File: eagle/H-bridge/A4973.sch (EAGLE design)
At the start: 13 parts, among them IC1 A4973DIL, X1 Load, X2 V_Load, X3 MODE, X4 332-02, X5 332-02

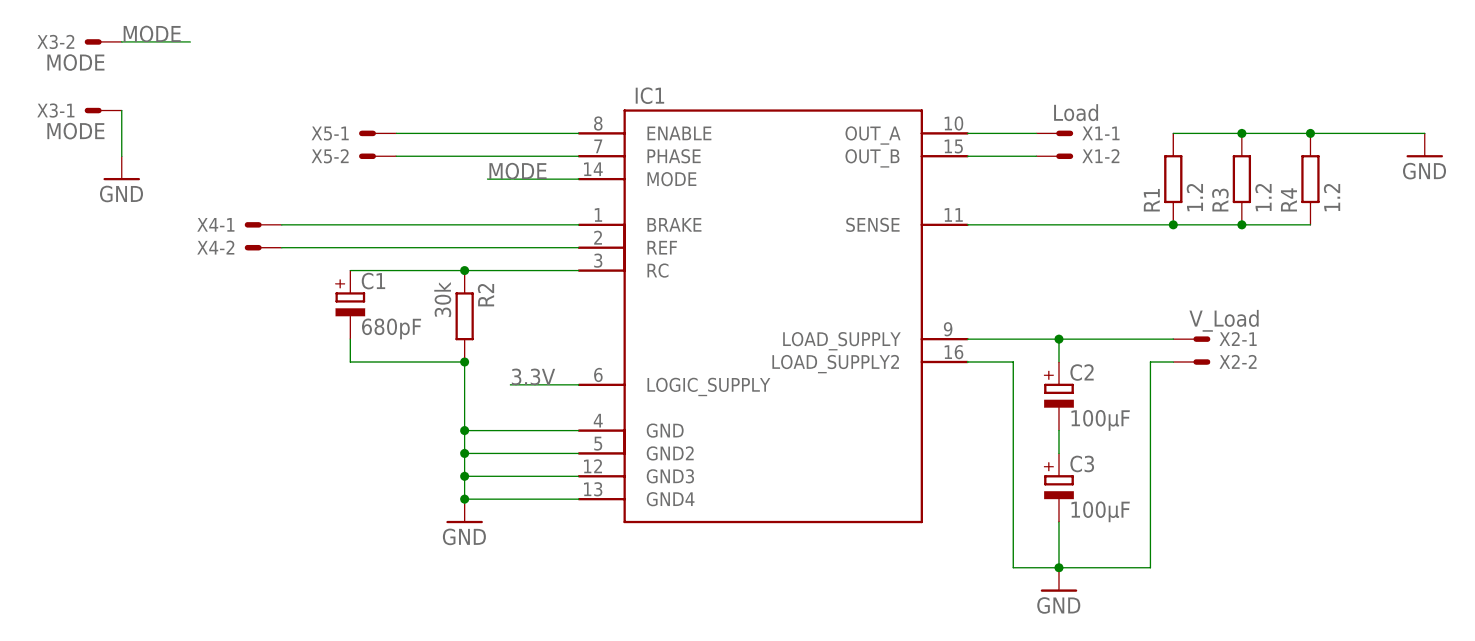
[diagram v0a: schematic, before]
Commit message: Added 3.3 v to IC. Made one load pin floating
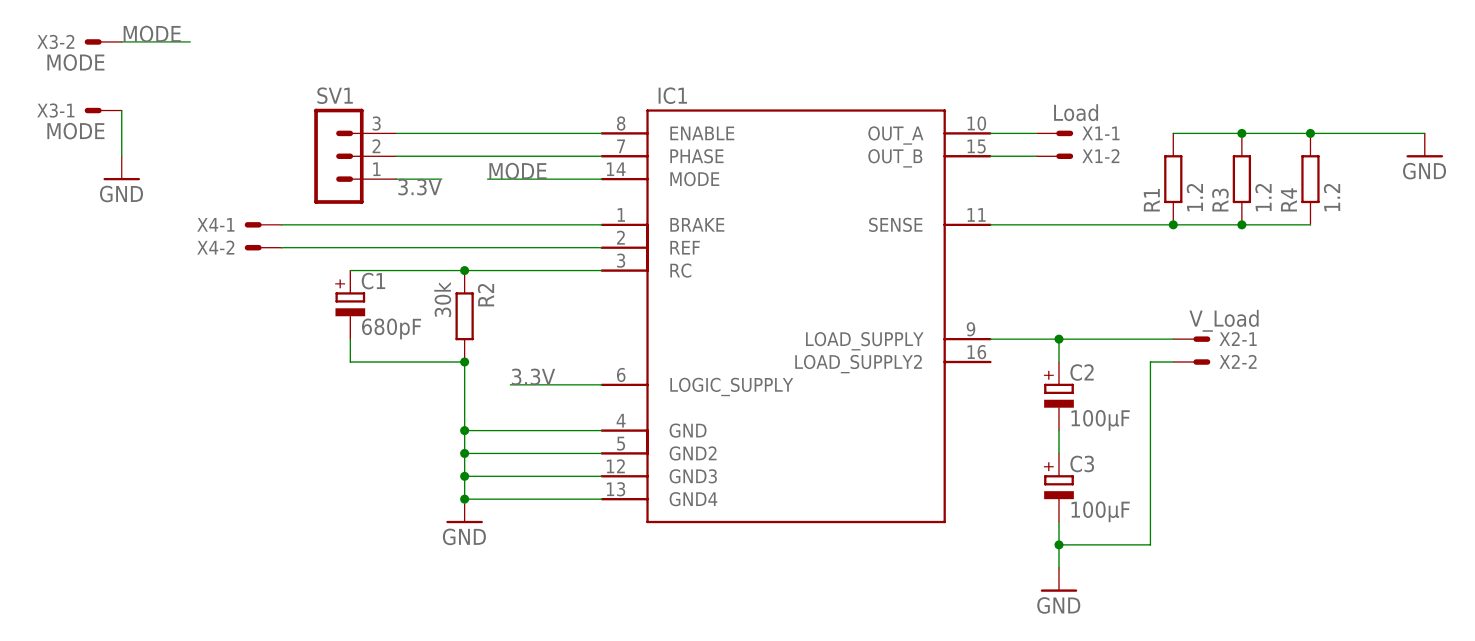
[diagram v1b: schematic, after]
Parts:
- removed X5: 332-02, con-garry:332-02
- added SV1: (no value), con-lstb:MA03-1
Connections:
- net 3.3V: now also SV1.1
- net GND: no longer IC1.LOAD_SUPPLY2
- net N$1: now also SV1.3; no longer X5-1.S
- net N$2: now also SV1.2; no longer X5-2.S
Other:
- moved on the sheet: IC1
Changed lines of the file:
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@@
 <part name="X3" library="con-garry" deviceset="332-02" device="" value="MODE"/>
 <part name="X4" library="con-garry" deviceset="332-02" device="" value=""/>
-<part name="X5" library="con-garry" deviceset="332-02" device="" value=""/>
+<part name="SV1" library="con-lstb" deviceset="MA03-1" device=""/>
 </parts>
 <sheets>
@@
 </plain>
 <instances>
-<instance part="IC1" gate="G$1" x="0" y="12.7"/>
+<instance part="IC1" gate="G$1" x="2.54" y="12.7"/>
 <instance part="GND1" gate="1" x="-17.78" y="-12.7"/>
 <instance part="X1" gate="-1" x="48.26" y="30.48"/>
@@
 <instance part="X4" gate="-1" x="-40.64" y="20.32" rot="R180"/>
 <instance part="X4" gate="-2" x="-40.64" y="17.78" rot="R180"/>
-<instance part="X5" gate="-1" x="-27.94" y="30.48" rot="R180"/>
-<instance part="X5" gate="-2" x="-27.94" y="27.94" rot="R180"/>
+<instance part="SV1" gate="G$1" x="-33.02" y="27.94"/>
 </instances>
 <busses>
@@
 <segment>
 <pinref part="IC1" gate="G$1" pin="GND"/>
-<wire x1="-5.08" y1="-2.54" x2="-17.78" y2="-2.54" width="0.1524" layer="91"/>
+<wire x1="-2.54" y1="-2.54" x2="-17.78" y2="-2.54" width="0.1524" layer="91"/>
 <wire x1="-17.78" y1="-2.54" x2="-17.78" y2="-5.08" width="0.1524" layer="91"/>
 <pinref part="IC1" gate="G$1" pin="GND4"/>
 <wire x1="-17.78" y1="-5.08" x2="-17.78" y2="-7.62" width="0.1524" layer="91"/>
 <wire x1="-17.78" y1="-7.62" x2="-17.78" y2="-10.16" width="0.1524" layer="91"/>
-<wire x1="-17.78" y1="-10.16" x2="-5.08" y2="-10.16" width="0.1524" layer="91"/>
+<wire x1="-17.78" y1="-10.16" x2="-2.54" y2="-10.16" width="0.1524" layer="91"/>
 <pinref part="IC1" gate="G$1" pin="GND3"/>
-<wire x1="-5.08" y1="-7.62" x2="-17.78" y2="-7.62" width="0.1524" layer="91"/>
+<wire x1="-2.54" y1="-7.62" x2="-17.78" y2="-7.62" width="0.1524" layer="91"/>
 <junction x="-17.78" y="-7.62"/>
 <pinref part="IC1" gate="G$1" pin="GND2"/>
-<wire x1="-5.08" y1="-5.08" x2="-17.78" y2="-5.08" width="0.1524" layer="91"/>
+<wire x1="-2.54" y1="-5.08" x2="-17.78" y2="-5.08" width="0.1524" layer="91"/>
 <junction x="-17.78" y="-5.08"/>
 <pinref part="GND1" gate="1" pin="GND"/>
@@
 </segment>
 <segment>
-<pinref part="IC1" gate="G$1" pin="LOAD_SUPPLY2"/>
-<wire x1="38.1" y1="5.08" x2="43.18" y2="5.08" width="0.1524" layer="91"/>
-<wire x1="43.18" y1="5.08" x2="43.18" y2="-17.78" width="0.1524" layer="91"/>
-<wire x1="43.18" y1="-17.78" x2="48.26" y2="-17.78" width="0.1524" layer="91"/>
-<wire x1="48.26" y1="-17.78" x2="58.42" y2="-17.78" width="0.1524" layer="91"/>
-<wire x1="58.42" y1="-17.78" x2="58.42" y2="5.08" width="0.1524" layer="91"/>
+<pinref part="C3" gate="G$1" pin="-"/>
+<pinref part="GND3" gate="1" pin="GND"/>
+<wire x1="48.26" y1="-17.78" x2="48.26" y2="-15.24" width="0.1524" layer="91"/>
 <pinref part="X2" gate="-2" pin="S"/>
-<wire x1="58.42" y1="5.08" x2="60.96" y2="5.08" width="0.1524" layer="91"/>
-<junction x="48.26" y="-17.78"/>
-<pinref part="GND3" gate="1" pin="GND"/>
-<wire x1="48.26" y1="-17.78" x2="48.26" y2="-12.7" width="0.1524" layer="91"/>
-<pinref part="C3" gate="G$1" pin="-"/>
+<wire x1="48.26" y1="-15.24" x2="48.26" y2="-12.7" width="0.1524" layer="91"/>
+<wire x1="60.96" y1="5.08" x2="58.42" y2="5.08" width="0.1524" layer="91"/>
+<wire x1="58.42" y1="5.08" x2="58.42" y2="-15.24" width="0.1524" layer="91"/>
+<wire x1="58.42" y1="-15.24" x2="48.26" y2="-15.24" width="0.1524" layer="91"/>
+<junction x="48.26" y="-15.24"/>
 </segment>
 <segment>
@@
 <pinref part="IC1" gate="G$1" pin="OUT_A"/>
 <pinref part="X1" gate="-1" pin="S"/>
-<wire x1="38.1" y1="30.48" x2="45.72" y2="30.48" width="0.1524" layer="91"/>
+<wire x1="40.64" y1="30.48" x2="45.72" y2="30.48" width="0.1524" layer="91"/>
 </segment>
 </net>
@@
 <pinref part="X1" gate="-2" pin="S"/>
 <pinref part="IC1" gate="G$1" pin="OUT_B"/>
-<wire x1="45.72" y1="27.94" x2="38.1" y2="27.94" width="0.1524" layer="91"/>
+<wire x1="45.72" y1="27.94" x2="40.64" y2="27.94" width="0.1524" layer="91"/>
 </segment>
 </net>
@@
 <pinref part="R1" gate="G$1" pin="1"/>
 <pinref part="IC1" gate="G$1" pin="SENSE"/>
-<wire x1="60.96" y1="20.32" x2="38.1" y2="20.32" width="0.1524" layer="91"/>
+<wire x1="60.96" y1="20.32" x2="40.64" y2="20.32" width="0.1524" layer="91"/>
 <pinref part="R3" gate="G$1" pin="1"/>
 <wire x1="60.96" y1="20.32" x2="68.58" y2="20.32" width="0.1524" layer="91"/>
@@
 <pinref part="IC1" gate="G$1" pin="RC"/>
 <pinref part="C1" gate="G$1" pin="+"/>
-<wire x1="-5.08" y1="15.24" x2="-17.78" y2="15.24" width="0.1524" layer="91"/>
+<wire x1="-2.54" y1="15.24" x2="-17.78" y2="15.24" width="0.1524" layer="91"/>
 <pinref part="R2" gate="G$1" pin="1"/>
 <wire x1="-17.78" y1="15.24" x2="-30.48" y2="15.24" width="0.1524" layer="91"/>
@@
 <net name="N$8" class="0">
 <segment>
+<pinref part="IC1" gate="G$1" pin="LOAD_SUPPLY"/>
+<pinref part="C2" gate="G$1" pin="+"/>
+<wire x1="48.26" y1="7.62" x2="40.64" y2="7.62" width="0.1524" layer="91"/>
+<wire x1="48.26" y1="5.08" x2="48.26" y2="7.62" width="0.1524" layer="91"/>
 <pinref part="X2" gate="-1" pin="S"/>
-<pinref part="IC1" gate="G$1" pin="LOAD_SUPPLY"/>
 <wire x1="60.96" y1="7.62" x2="48.26" y2="7.62" width="0.1524" layer="91"/>
-<pinref part="C2" gate="G$1" pin="+"/>
-<wire x1="48.26" y1="7.62" x2="38.1" y2="7.62" width="0.1524" layer="91"/>
-<wire x1="48.26" y1="5.08" x2="48.26" y2="7.62" width="0.1524" layer="91"/>
 <junction x="48.26" y="7.62"/>
 </segment>
@@
 <segment>
 <pinref part="IC1" gate="G$1" pin="LOGIC_SUPPLY"/>
-<wire x1="-12.7" y1="2.54" x2="-5.08" y2="2.54" width="0.1524" layer="91"/>
+<wire x1="-12.7" y1="2.54" x2="-2.54" y2="2.54" width="0.1524" layer="91"/>
 <label x="-12.7" y="2.54" size="1.778" layer="95"/>
+</segment>
+<segment>
+<pinref part="SV1" gate="G$1" pin="1"/>
+<wire x1="-25.4" y1="25.4" x2="-20.32" y2="25.4" width="0.1524" layer="91"/>
+<label x="-20.32" y="25.4" size="1.778" layer="95" rot="R180"/>
 </segment>
 </net>
@@
 <segment>
 <pinref part="IC1" gate="G$1" pin="BRAKE"/>
-<wire x1="-5.08" y1="20.32" x2="-38.1" y2="20.32" width="0.1524" layer="91"/>
+<wire x1="-2.54" y1="20.32" x2="-38.1" y2="20.32" width="0.1524" layer="91"/>
 <pinref part="X4" gate="-1" pin="S"/>
 </segment>
@@
 <segment>
 <pinref part="IC1" gate="G$1" pin="REF"/>
-<wire x1="-5.08" y1="17.78" x2="-38.1" y2="17.78" width="0.1524" layer="91"/>
+<wire x1="-2.54" y1="17.78" x2="-38.1" y2="17.78" width="0.1524" layer="91"/>
 <pinref part="X4" gate="-2" pin="S"/>
-</segment>
-</net>
-<net name="N$1" class="0">
-<segment>
-<pinref part="IC1" gate="G$1" pin="ENABLE"/>
-<wire x1="-25.4" y1="30.48" x2="-5.08" y2="30.48" width="0.1524" layer="91"/>
-<pinref part="X5" gate="-1" pin="S"/>
-</segment>
-</net>
-<net name="N$2" class="0">
-<segment>
-<pinref part="IC1" gate="G$1" pin="PHASE"/>
-<wire x1="-5.08" y1="27.94" x2="-25.4" y2="27.94" width="0.1524" layer="91"/>
-<pinref part="X5" gate="-2" pin="S"/>
 </segment>
 </net>
@@
 <segment>
 <pinref part="IC1" gate="G$1" pin="MODE"/>
-<wire x1="-5.08" y1="25.4" x2="-15.24" y2="25.4" width="0.1524" layer="91"/>
+<wire x1="-2.54" y1="25.4" x2="-15.24" y2="25.4" width="0.1524" layer="91"/>
 <label x="-15.24" y="25.4" size="1.778" layer="95"/>
 </segment>
@@
 </segment>
 </net>
+<net name="N$1" class="0">
+<segment>
+<pinref part="SV1" gate="G$1" pin="3"/>
+<pinref part="IC1" gate="G$1" pin="ENABLE"/>
+<wire x1="-25.4" y1="30.48" x2="-2.54" y2="30.48" width="0.1524" layer="91"/>
+</segment>
+</net>
+<net name="N$2" class="0">
+<segment>
+<pinref part="IC1" gate="G$1" pin="PHASE"/>
+<pinref part="SV1" gate="G$1" pin="2"/>
+<wire x1="-2.54" y1="27.94" x2="-25.4" y2="27.94" width="0.1524" layer="91"/>
+</segment>
+</net>
